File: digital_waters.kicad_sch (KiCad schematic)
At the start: 9 parts, among them U1 MCP3208, U2 M24C02-FMN

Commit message: Prototype v0.3.1 WIP Just a maintenance checkin. Many changes - Removed the Base Sensor schematic and put all sensors into SensorPrototype - Added a constant current LED driver for camera illumination - Added a 12V buck converter to the input in support of external power - Added a low-side current sense to the input - Added an LDO regulator to cleanup Buck output and to provide battery regulation - Added support for an internal battery + switchover / charge circuit. - Swapped headers for proper board connectors - Added an RS485 transceiver for external + modem communication - Added an additional temperature circuit in support of NTC probes - Incorporated the AS Dissolved Oxygen sensor into the main board - Added DC return path resistors to non-inverting amps - Fixed mixed power domain bug - Moved AS isolated carrier board to 3.3V rail and routed the shutdown pin to en/sh - Moved the DHT20 to the 3.3V rail - In the process of re-routing ADC channels.
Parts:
- removed C31: 1u, Capacitor_SMD:C_1210_3225Metric_Pad1.33x2.70mm_HandSolder, symbol Device:C
- removed C32: 0.1u, Capacitor_SMD:C_1210_3225Metric_Pad1.33x2.70mm_HandSolder, symbol Device:C
- removed R38, R39: 10k, Resistor_SMD:R_1210_3225Metric_Pad1.30x2.65mm_HandSolder, symbol Device:R
- removed U2: M24C02-FMN, Package_SO:SOIC-8_3.9x4.9mm_P1.27mm, symbol Memory_EEPROM:M24C02-FMN
- added J1: Conn_01x02, Connector_JST:JST_ZH_S2B-ZR-SM4A-TF_1x02-1MP_P1.50mm_Horizontal, symbol Connector_Generic:Conn_01x02
- added J2: Conn_01x04, Connector_JST:JST_ZH_S4B-ZR-SM4A-TF_1x04-1MP_P1.50mm_Horizontal, symbol Connector_Generic:Conn_01x04
- added J3, J4: Conn_01x07, Connector_JST:JST_ZH_S7B-ZR-SM4A-TF_1x07-1MP_P1.50mm_Horizontal, symbol Connector_Generic:Conn_01x07
- added R14: 100, symbol Device:R
- added U10: ST485E, Package_SO:SOIC-8_3.9x4.9mm_P1.27mm, symbol Interface_UART:ST485E
- added U3: ESDA5V3SC5, Package_TO_SOT_SMD:SOT-23-5, symbol AndrewAdditions:sda5v3sc6_split
- C33, C34, C35: footprint Capacitor_SMD:C_1210_3225Metric_Pad1.33x2.70mm_HandSolder -> Capacitor_SMD:C_0805_2012Metric_Pad1.18x1.45mm_HandSolder
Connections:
- net +5V: now also U10.8 (VCC)
- net GNDA: no longer C33.2, C34.2, C35.2
- net GNDD: now also U10.5 (GND), U3.2, U3.2
- net SPI_CS0: no longer U1.10 (~{CS}/SHDN)
- net SPI_MOSI: no longer U1.11 (Din)
- net +VSW: no longer names the net of C34.1, C35.1
- net +VSW: no longer U1.16 (Vdd)
- net ADC.CAL: no longer names the net of U1.1 (CH0)
- net ADC.DO: no longer names the net of U1.3 (CH2)
- net ADC.ORP: no longer names the net of U1.5 (CH4)
- net ADC.PH: no longer names the net of U1.4 (CH3)
- net ADC.TEMP: no longer names the net of U1.7 (CH6)
- net ADC.TURB: no longer names the net of U1.2 (CH1)
- net ADC.VBATT: no longer names the net of U1.6 (CH5)
- net VDDA: no longer names the net of C33.1
- net VDDA: no longer U1.15 (Vref)
- new net: C33.2, C34.2, C35.2
- new net GPIO_1_U0TXD: U10.4 (DI)
- new net GPIO_32_COM_DE/RE*: U10.2 (~{RE}), U10.3 (DE)
- new net GPIO_3_U0RXD: U10.1 (RO)
- new net INPUT_OUTPUT_RS485_A: R14.1, U10.6 (A), U3.1
- new net INPUT_OUTPUT_RS485_B: R14.2, U10.7 (B), U3.3
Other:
- removed sheet Base_Sensor
- sheet Micocontroller ports: added COM_DE/RE*, OUTPUT_ILLUMINATOR+, OUTPUT_ILLUMINATOR-, RXD, TXD; removed ADC_TEMP
- sheet Power ports: added +5V_SW, ADC_ISENSE, INPUT_12V+, INPUT_12V-, INPUT_VBATT_+, INPUT_VBATT_-; removed +2.5V_REF, +4.096_REF, VDD
- sheet Sensor Module Prototype ports: added +4.096_REF_BUF_A, ADC_CAL, ADC_TEMP_NTC_10k, ADC_TEMP_PT_1000, EN/~{SH_0}, INPUT_DO, INPUT_NTC10K, INPUT_ORP+, INPUT_ORP-, INPUT_PT1000+, INPUT_PT1000-, INPUT_TURB_SIG, INPUT_TURB_V+, INPUT_TURB_V-, INPUT_pH+, INPUT_pH-; removed +2.5V_REF
- note added: "Using Cat5 cable, the characteristic impedance is 100 Ohm. Adding a DC termination resistor of 100 Ohm to both ends of the cable should suffice for termination. This adds a DC load to the drivers though and you should consider designing an AC termination instead (Rt in series with a cap -- this messes up the rise and fall times though so you have to do it carefully)."
- note removed: "Address: 0xA0 [0b1010 0(p3) 0(p2) 0(p1) R/*W]"
- note removed: "I2C ADDR 0bXXX 000X"
- note removed: "Pullups on I2C Lines may not be necessary"
- moved on the sheet: C33, C34, C35, U1

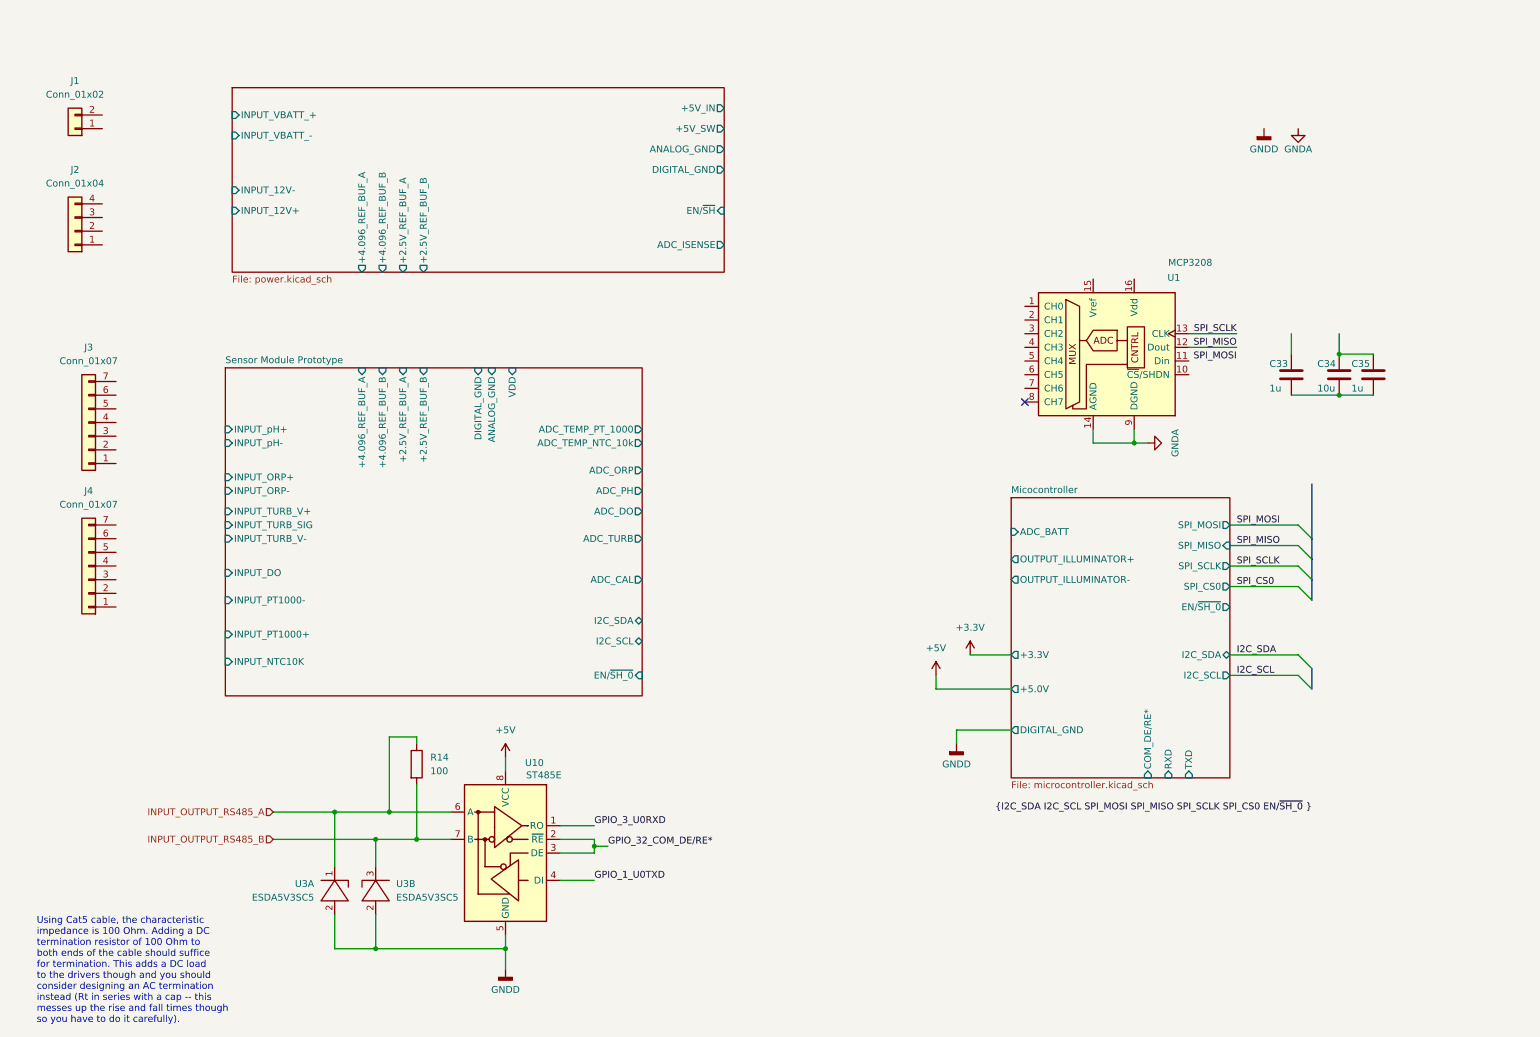
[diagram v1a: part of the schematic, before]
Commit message: Board V0.0.3 Everything is routed and connected ERC and DRC run without serious error. (There are DRC violations due to a VSSP-83x3mm package but I'm not sure why)
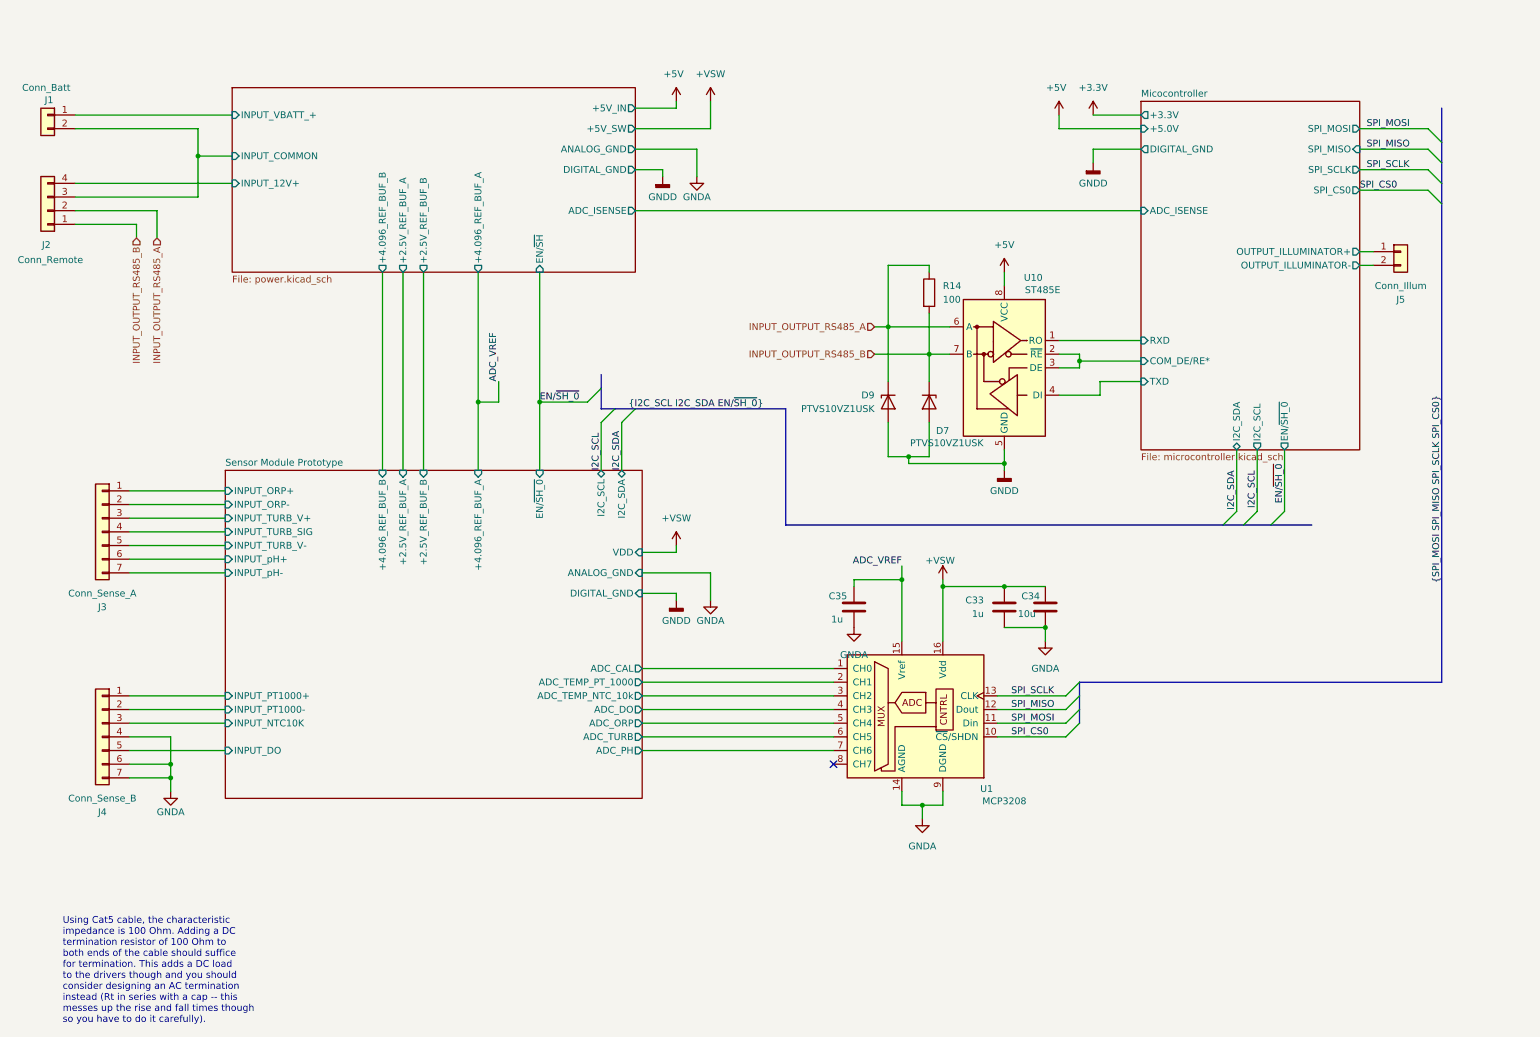
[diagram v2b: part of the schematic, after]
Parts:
- removed U3: ESDA5V3SC5, Package_TO_SOT_SMD:SOT-23-5, symbol AndrewAdditions:sda5v3sc6_split
- added D7, D9: PTVS10VZ1USK, Diode_SMD:Nexperia_DSN1608-2_1.6x0.8mm, symbol Diode:PTVS10VZ1USK
- added J5: Conn_Illum, Connector_JST:JST_ZH_S2B-ZR-SM4A-TF_1x02-1MP_P1.50mm_Horizontal, symbol Connector_Generic:Conn_01x02
- J1: value Conn_01x02 -> Conn_Batt
- J2: value Conn_01x04 -> Conn_Remote
- J3: value Conn_01x07 -> Conn_Sense_A
- J4: value Conn_01x07 -> Conn_Sense_B
- R14: footprint (none) -> Resistor_SMD:R_0805_2012Metric_Pad1.20x1.40mm_HandSolder
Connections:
- net GPIO_1_U0TXD is gone; now on net Micocontroller/TXD: U10.4 (DI)
- net GPIO_32_COM_DE/RE* is gone; now on net Micocontroller/COM_DE/RE*: U10.2 (~{RE}), U10.3 (DE)
- net GPIO_3_U0RXD is gone; now on net Micocontroller/RXD: U10.1 (RO)
- net GNDA: now also C33.2, C34.2, C35.2, J4.4 (Pin_4), J4.6 (Pin_6), J4.7 (Pin_7)
- net GNDD: now also D7.2 (A), D9.2 (A)
- net INPUT_OUTPUT_RS485_A: now also J2.2 (Pin_2), D9.1 (K)
- net INPUT_OUTPUT_RS485_B: now also J2.1 (Pin_1), D7.1 (K)
- net Micocontroller/OUTPUT_ILLUMINATOR+: now also J5.1 (Pin_1)
- net Micocontroller/OUTPUT_ILLUMINATOR-: now also J5.2 (Pin_2)
- net Power/INPUT_12V+: now also J2.4 (Pin_4)
- net Power/INPUT_VBATT_+: now also J1.1 (Pin_1)
- net SPI_CS0: now also U1.10 (~{CS}/SHDN)
- net SPI_MOSI: now also U1.11 (Din)
- net Sensor Module Prototype/ADC_CAL: now also U1.1 (CH0)
- net Sensor Module Prototype/ADC_DO: now also U1.4 (CH3)
- net Sensor Module Prototype/ADC_ORP: now also U1.5 (CH4)
- net Sensor Module Prototype/ADC_PH: now also U1.7 (CH6)
- net Sensor Module Prototype/ADC_TEMP_NTC_10k: now also U1.3 (CH2)
- net Sensor Module Prototype/ADC_TEMP_PT_1000: now also U1.2 (CH1)
- net Sensor Module Prototype/ADC_TURB: now also U1.6 (CH5)
- net Sensor Module Prototype/INPUT_DO: now also J4.5 (Pin_5)
- net Sensor Module Prototype/INPUT_NTC10K: now also J4.3 (Pin_3)
- net Sensor Module Prototype/INPUT_ORP+: now also J3.1 (Pin_1)
- net Sensor Module Prototype/INPUT_ORP-: now also J3.2 (Pin_2)
- net Sensor Module Prototype/INPUT_PT1000-: now also J4.2 (Pin_2)
- net Sensor Module Prototype/INPUT_TURB_SIG: now also J3.4 (Pin_4)
- net Sensor Module Prototype/INPUT_TURB_V+: now also J3.3 (Pin_3)
- net Sensor Module Prototype/INPUT_TURB_V-: now also J3.5 (Pin_5)
- net Sensor Module Prototype/INPUT_pH+: now also J3.6 (Pin_6)
- net Sensor Module Prototype/INPUT_pH-: now also J3.7 (Pin_7)
- net Power/INPUT_COMMON: now reaches J2.3 (Pin_3)
- net Power/INPUT_COMMON: now also J1.2 (Pin_2)
- net +VSW: now reaches C34.1
- net +VSW: now also C33.1, U1.16 (Vdd); no longer C35.1
- net ADC_VREF: now reaches U1.15 (Vref)
- net ADC_VREF: now also C35.1
- net Sensor Module Prototype/INPUT_PT1000+: now reaches J4.1 (Pin_1)
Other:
- sheet Micocontroller ports: added ADC_ISENSE; removed ADC_BATT
- sheet Power ports: added INPUT_COMMON; removed INPUT_12V-, INPUT_VBATT_-
- moved on the sheet: J1, J2, J3, J4, R14, U1, U10

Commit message: BUG FIX -------- There were some issues with the board WRT manufacturing. I changed the VSSOP 8 packages to SOT versions and re-routed
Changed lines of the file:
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@@
+	(wire
+		(pts
+			(xy 138.43 193.04) (xy 147.32 193.04)
+		)
+		(stroke
+			(width 0)
+			(type default)
+		)
+	)
 	(wire
 		(pts
@@
 	(wire
 		(pts
+			(xy 147.32 193.04) (xy 147.32 189.23)
+		)
+		(stroke
+			(width 0)
+			(type default)
+		)
+	)
+	(wire
+		(pts
 			(xy 124.46 81.28) (xy 124.46 90.17)
 		)
@@
 		(pts
 			(xy 185.42 81.28) (xy 185.42 87.63)
+		)
+		(stroke
+			(width 0)
+			(type default)
+		)
+	)
+	(wire
+		(pts
+			(xy 138.43 190.5) (xy 138.43 193.04)
 		)
 		(stroke
@@
 			)
 			(justify left bottom)
+		)
+	)
+	(label "ADC_VREF"
+		(at 138.43 190.5 180)
+		(effects
+			(font
+				(size 1.27 1.27)
+			)
+			(justify right bottom)
 		)
 	)
@@
 					(unit 1)
 				)
+			)
+		)
+	)
+	(symbol
+		(lib_id "power:PWR_FLAG")
+		(at 147.32 189.23 0)
+		(unit 1)
+		(exclude_from_sim no)
+		(in_bom yes)
+		(on_board yes)
+		(dnp no)
+		(fields_autoplaced yes)
+		(property "Reference" "#FLG6"
+			(at 147.32 187.325 0)
+			(effects
+				(font
+					(size 1.27 1.27)
+				)
+				(hide yes)
+			)
+		)
+		(property "Value" "PWR_FLAG"
+			(at 147.32 184.15 0)
+			(effects
+				(font
+					(size 1.27 1.27)
+				)
+			)
+		)
+		(property "Footprint" ""
+			(at 147.32 189.23 0)
+			(effects
+				(font
+					(size 1.27 1.27)
+				)
+				(hide yes)
+			)
+		)
+		(property "Datasheet" "~"
+			(at 147.32 189.23 0)
+			(effects
+				(font
+					(size 1.27 1.27)
+				)
+				(hide yes)
+			)
+		)
+		(property "Description" "Special symbol for telling ERC where power comes from"
+			(at 147.32 189.23 0)
+			(effects
+				(font
+					(size 1.27 1.27)
+				)
+				(hide yes)
+			)
+		)
+		(pin "1"
+		)
+		(instances
+			(project ""
+				(path "/37fdfe07-1a70-41c8-8af2-e03e19737580"
+					(reference "#FLG6")
+					(unit 1)
+				)

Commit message: Maintenance update - Adding the EC isolation board schematic - Added a harness page for wireing module together
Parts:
- added R4: 0 Ohm, Resistor_SMD:R_1206_3216Metric_Pad1.30x1.75mm_HandSolder, symbol Device:R
- C33, C35: MPN (none) -> CL21B105KOFNNNG; Manufacturer (none) -> Samsung; Package (none) -> 0805
- C34: MPN (none) -> CL21B106KPQNNNE; Manufacturer (none) -> Samsung; Package (none) -> 0805
- D7, D9: MPN (none) -> PTVS10VZ1USK; Manufacturer (none) -> Nexperia; Package (none) -> DSN1608-2
- J1, J2, J3, J4, J5: now not fitted
- R14: MPN (none) -> AC0805FR-7W100RL; Manufacturer (none) -> YAGEO; Package (none) -> 0805
- U1: MPN (none) -> MCP3208-CI/SL; Manufacturer (none) -> Microchip; Package (none) -> SOIC-16
- U10: MPN (none) -> ST485EBDR; Manufacturer (none) -> ST; Package (none) -> SOIC-8
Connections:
- new net ANALOG_GND: R4.2
- new net DIGITAL_GND: R4.1
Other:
- added sheet Harness (Harness.kicad_sch)
- note added: "AGND and DGND are tied together internally to the MCP320X. This connection should be as close to thay chip as possible."
- note added: "ERC Overrides"
- note added: "RS-485 transceiver: Using Cat5 cable, the characteristic impedance is 100 Ohm. Adding a DC termination resistor of 100 Ohm to both ends of the cable should suffice for termination. This adds a DC load to the drivers though and you should consider designing an AC termination instead (Rt in series with a cap -- this messes up the rise and fall times though so you have to do it carefully)."
- note removed: "Using Cat5 cable, the characteristic impedance is 100 Ohm. Adding a DC termination resistor of 100 Ohm to both ends of the cable should suffice for termination. This adds a DC load to the drivers though and you should consider designing an AC termination instead (Rt in series with a cap -- this messes up the rise and fall times though so you have to do it carefully)."
